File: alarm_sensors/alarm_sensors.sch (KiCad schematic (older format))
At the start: 60 parts, among them J1 ZONE 1, J10 ZONE 10, J11 PWR, J12 Debug, J2 ZONE 2, J3 ZONE 3, J4 Z 4, J5 Z 5, J6 Z 6, J7 Z 7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

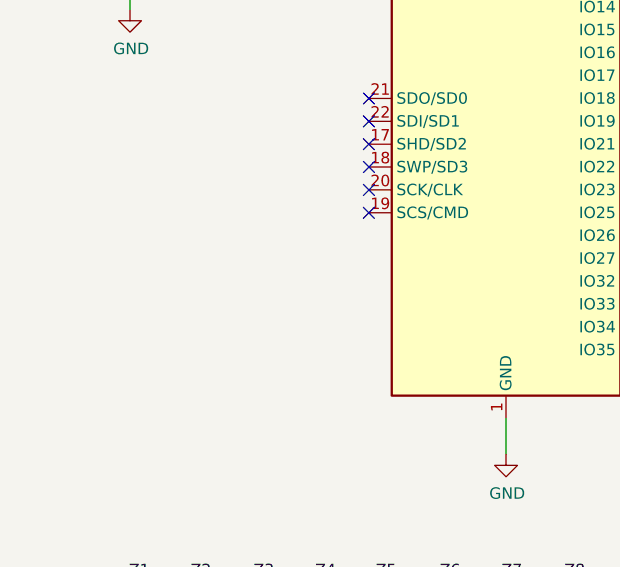
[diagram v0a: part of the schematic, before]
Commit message: Fix alam-sensor button input
GPIO35 doesn't haave an internal pull-up, move to GPIO32.
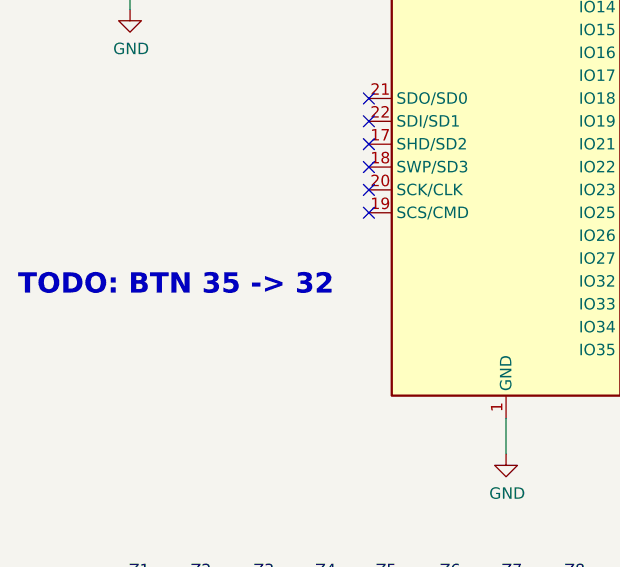
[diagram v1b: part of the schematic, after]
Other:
- note added: "TODO: BTN 35 -> 32"
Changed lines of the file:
@@
 Wire Wire Line
 	9690 1210 9690 1600
+Text Notes 645  3760 0    89   ~ 18
+TODO: BTN 35 -> 32
 $EndSCHEMATC
